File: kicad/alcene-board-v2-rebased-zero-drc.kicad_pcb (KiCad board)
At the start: 2 copper layers, 123 x 90 mm, 16 parts, among them J1 ESP32-S3-DevKitC-1_J1, J2 USB-C Input, J3 ESP32-S3-DevKitC-1_J3, J4 ILI9341_TFT_14pin, J5 Male Pin Header 1x18 - J1 Sig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, J6 Male Pin Header 1x18 - J3 Sig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, J7 Male Pin Header 2x4 - GND, J8 Male Pin Header 2x4 - 3V3, J9 Male Pin Header 2x4 - VIN 5V, SW1 ESP32-S3 Reset (NO momentary)

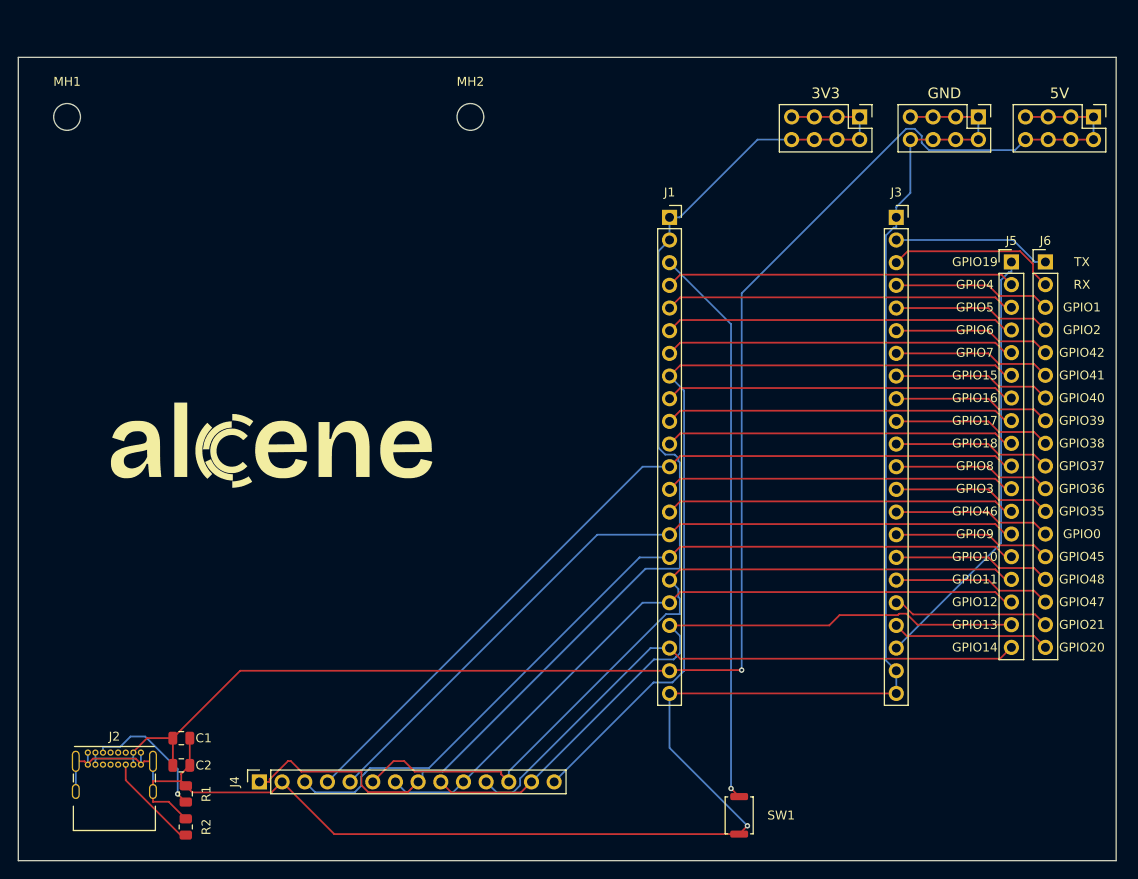
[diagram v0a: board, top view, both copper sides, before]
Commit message: feat: Update component positions and increase fabrication line widths in PCB l
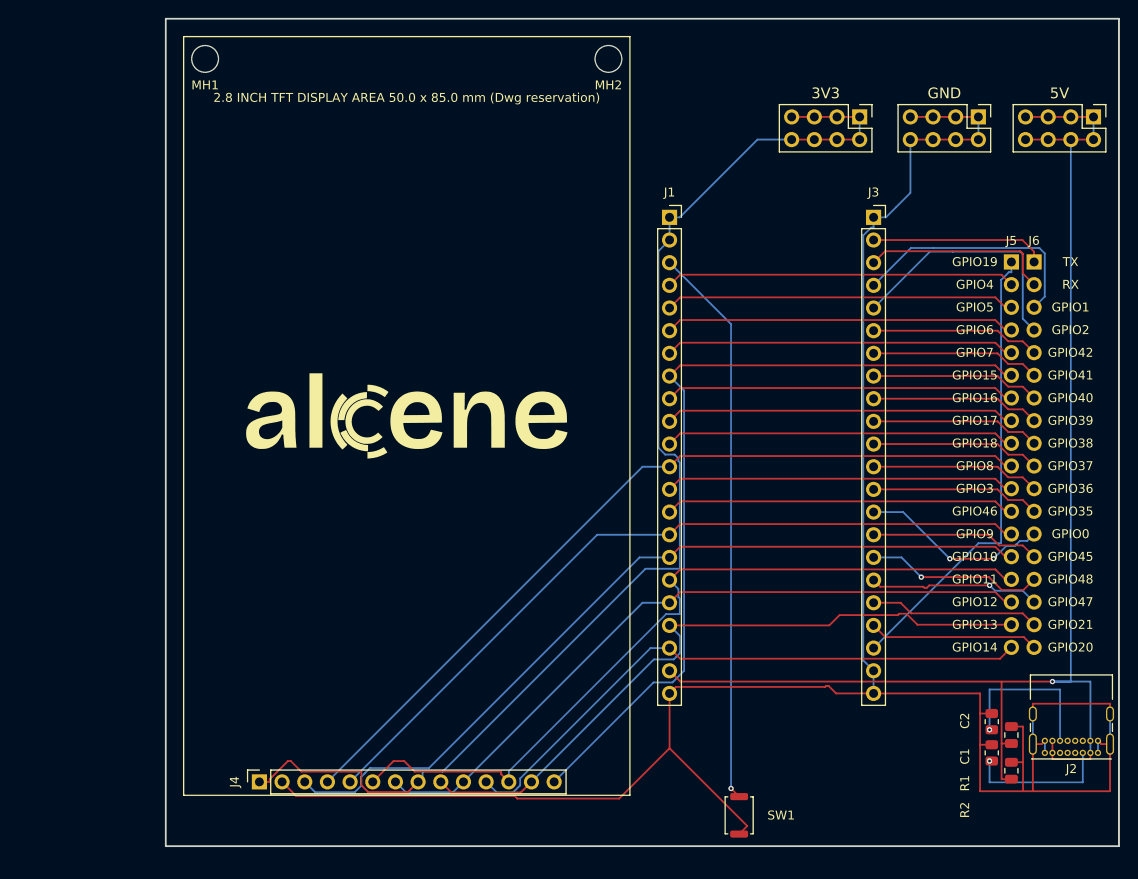
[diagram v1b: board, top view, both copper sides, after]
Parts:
- moved J2 113.2 mm to (154.7, 110.0), turned to 180 degrees
- moved C1 93.1 mm to (145.0, 112.0), turned to 90 degrees
- moved C2 93.1 mm to (145.0, 108.0), turned to 90 degrees
- moved R2 91.1 mm to (142.8, 106.5)
- moved R1 90.4 mm to (142.8, 110.0)
- moved MH2 16.8 mm to (99.9, 32.2)
- moved MH1 16.8 mm to (54.7, 32.2)
- moved J3 2.54 mm to (129.6, 50.0)
- moved J6 1.27 mm to (147.5, 55.0)
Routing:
- net GND: track 226.9 -> 257.2 mm, vias 1 -> 0
- net VIN: track 183.4 -> 156.3 mm
- net GPIO2: track 17.7 -> 28.5 mm
- net GPIO1: track 17.7 -> 27.7 mm
- net Net-(J2-PadB5): track 11.0 -> 18.2 mm, vias 0 -> 1
- net GPIO0: track 17.7 -> 21.3 mm, vias 0 -> 2
- net GPIO19: track 48.8 -> 51.3 mm
- net GPIO48: track 17.7 -> 20.0 mm, vias 0 -> 1
- net RX: track 19.3 -> 21.4 mm
- net TX: track 17.7 -> 19.7 mm
- net GPIO47: track 17.7 -> 19.2 mm, vias 0 -> 1
- net GPIO21: track 17.7 -> 19.0 mm
- net GPIO45: track 17.7 -> 19.0 mm
- net GPIO38: track 17.7 -> 19.0 mm
- net GPIO36: track 17.7 -> 19.0 mm
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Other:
- board size 123 x 90 mm -> 106.8 x 92.7 mm
- board text added: "2.8 INCH TFT DISPLAY AREA 50.0 x 85.0 mm (Dwg reservation)"
- board text removed: "2.8 INCH TFT DISPLAY AREA 49.8 x 78.5 mm (Dwg reservation)"

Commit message: feat: Align power breakout headers and update project configuration
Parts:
- moved J8 13.7 mm to (114.3, 38.8)
- moved J7 10.4 mm to (130.9, 38.8)
- moved J9 6.66 mm to (147.5, 38.8)
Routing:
- net 3V3: track 137.9 -> 129.3 mm
- net VIN: track 156.3 -> 160.5 mm
- net GND: track 257.2 -> 260.9 mm
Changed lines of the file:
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@@
 	(footprint "Connector_PinHeader_2.54mm:PinHeader_2x04_P2.54mm_Vertical"
 		(layer "F.Cu")
-		(at 128 38.75 -90)
+		(at 114.32 38.75 -90)
 		(descr "Through hole straight pin header, 2x04, 2.54mm pitch, double rows")
 		(tags "Through hole pin header THT 2x04 2.54mm double row")
@@
 	(footprint "Connector_PinHeader_2.54mm:PinHeader_2x04_P2.54mm_Vertical"
 		(layer "F.Cu")
-		(at 141.3 38.75 -90)
+		(at 130.93 38.75 -90)
 		(descr "Through hole straight pin header, 2x04, 2.54mm pitch, double rows")
 		(tags "Through hole pin header THT 2x04 2.54mm double row")
@@
 	(footprint "Connector_PinHeader_2.54mm:PinHeader_2x04_P2.54mm_Vertical"
 		(layer "F.Cu")
-		(at 154.2 38.75 -90)
+		(at 147.54 38.75 -90)
 		(descr "Through hole straight pin header, 2x04, 2.54mm pitch, double rows")
 		(tags "Through hole pin header THT 2x04 2.54mm double row")
@@
 	)
 	(gr_text "3V3"
-		(at 124.19 36.1 0)
+		(at 110.51 36.1 0)
 		(layer "F.SilkS")
 		(effects
@@
 	)
 	(gr_text "GND"
-		(at 137.49 36.1 0)
+		(at 127.12 36.1 0)
 		(layer "F.SilkS")
 		(effects
@@
 	)
 	(gr_text "5V"
-		(at 150.39 36.1 0)
+		(at 143.73 36.1 0)
 		(layer "F.SilkS")
 		(effects
@@
 	)
 	(segment
-		(start 136.22 41.29)
-		(end 138.76 41.29)
-		(width 0.2)
-		(layer "F.Cu")
-		(net "GND")
-	)
-	(segment
-		(start 138.76 38.75)
-		(end 141.3 38.75)
-		(width 0.2)
-		(layer "F.Cu")
-		(net "GND")
-	)
-	(segment
 		(start 124.237 102.496)
 		(end 124.12 102.613)
@@
 	)
 	(segment
-		(start 138.76 41.29)
-		(end 141.3 41.29)
-		(width 0.2)
-		(layer "F.Cu")
-		(net "GND")
-	)
-	(segment
-		(start 136.22 38.75)
-		(end 138.76 38.75)
-		(width 0.2)
-		(layer "F.Cu")
-		(net "GND")
-	)
-	(segment
 		(start 64.8762 114.836)
 		(end 71.9021 114.836)
@@
 	)
 	(segment
-		(start 133.68 41.29)
-		(end 136.22 41.29)
-		(width 0.2)
-		(layer "F.Cu")
-		(net "GND")
-	)
-	(segment
 		(start 147.4 105.64)
 		(end 147.4 104.488)
@@
 	)
 	(segment
-		(start 133.68 38.75)
-		(end 136.22 38.75)
-		(width 0.2)
-		(layer "F.Cu")
-		(net "GND")
-	)
-	(segment
 		(start 89.3636 114.836)
 		(end 89.6451 115.118)
@@
 	)
 	(segment
-		(start 129.56 50)
-		(end 130.948 50)
-		(width 0.2)
-		(layer "B.Cu")
-		(net "GND")
-	)
-	(segment
-		(start 130.948 50)
-		(end 132.1 48.8483)
-		(width 0.2)
-		(layer "B.Cu")
-		(net "GND")
-	)
-	(segment
 		(start 148.75 108.65)
 		(end 148.75 110)
@@
 	)
 	(segment
-		(start 141.3 41.29)
-		(end 141.3 38.75)
-		(width 0.2)
-		(layer "B.Cu")
-		(net "GND")
-	)
-	(segment
 		(start 128.402 99.6419)
 		(end 129.56 100.8)
@@
 	)
 	(segment
-		(start 133.68 47.2683)
-		(end 132.1 48.8483)
-		(width 0.2)
-		(layer "B.Cu")
-		(net "GND")
-	)
-	(segment
 		(start 129.56 103.34)
 		(end 129.56 100.8)
@@
 	)
 	(segment
-		(start 133.68 41.29)
-		(end 133.68 47.2683)
-		(width 0.2)
-		(layer "B.Cu")
-		(net "GND")
-	)
-	(segment
 		(start 129.272 51.1517)
 		(end 128.402 52.0219)
@@
 	)
 	(segment
-		(start 146.58 41.29)
-		(end 149.12 41.29)
-		(width 0.2)
-		(layer "F.Cu")
-		(net "VIN")
-	)
-	(segment
-		(start 151.66 38.75)
-		(end 154.2 38.75)
-		(width 0.2)
-		(layer "F.Cu")
-		(net "VIN")
-	)
-	(segment
-		(start 149.12 41.29)
-		(end 151.66 41.29)
-		(width 0.2)
-		(layer "F.Cu")
-		(net "VIN")
-	)
-	(segment
-		(start 146.58 38.75)
-		(end 149.12 38.75)
-		(width 0.2)
-		(layer "F.Cu")
-		(net "VIN")
-	)
-	(segment
-		(start 151.66 41.29)
-		(end 154.2 41.29)
-		(width 0.2)
-		(layer "F.Cu")
-		(net "VIN")
-	)
-	(segment
-		(start 149.12 38.75)
-		(end 151.66 38.75)
-		(width 0.2)
-		(layer "F.Cu")
-		(net "VIN")
-	)
-	(segment
 		(start 106.7 100.8)
 		(end 107.913 102.013)
@@
 	)
 	(segment
-		(start 154.2 41.29)
-		(end 154.2 38.75)
-		(width 0.2)
-		(layer "B.Cu")
-		(net "VIN")
-	)
-	(segment
 		(start 151.66 41.29)
 		(end 151.66 102.013)
@@
 	)
 	(segment
-		(start 125.46 38.75)
-		(end 128 38.75)
-		(width 0.2)
-		(layer "F.Cu")
-		(net "3V3")
-	)
-	(segment
 		(start 64.2737 110.923)
 		(end 63.9409 110.923)
@@
 	)
 	(segment
-		(start 122.92 41.29)
-		(end 125.46 41.29)
-		(width 0.2)
-		(layer "F.Cu")
-		(net "3V3")
-	)
-	(segment
 		(start 72.18 113.634)
 		(end 72.18 112.1)
@@
 	)
 	(segment
-		(start 125.46 41.29)
-		(end 128 41.29)
-		(width 0.2)
-		(layer "F.Cu")
-		(net "3V3")
-	)
-	(segment
 		(start 60.75 113.25)
 		(end 61.9017 113.25)
@@
 	)
 	(segment
-		(start 122.92 38.75)
-		(end 125.46 38.75)
-		(width 0.2)
-		(layer "F.Cu")
-		(net "3V3")
-	)
-	(segment
-		(start 120.38 41.29)
-		(end 122.92 41.29)
-		(width 0.2)
-		(layer "F.Cu")
-		(net "3V3")
-	)
-	(segment
 		(start 72.9474 114.402)
 		(end 72.18 113.634)
@@
 	)
 	(segment
-		(start 120.38 38.75)
-		(end 122.92 38.75)
-		(width 0.2)
-		(layer "F.Cu")
-		(net "3V3")
-	)
-	(segment
 		(start 79.0271 112.1)
 		(end 81.2742 112.1)
@@
 	)
 	(segment
-		(start 106.7 50)
-		(end 107.852 50)
-		(width 0.2)
-		(layer "B.Cu")
-		(net "3V3")
-	)
-	(segment
 		(start 105.46 53.7799)
 		(end 106.7 52.54)
@@
 	)
 	(segment
-		(start 128 41.29)
-		(end 128 38.75)
-		(width 0.2)
-		(layer "B.Cu")
-		(net "3V3")
-	)
-	(segment
 		(start 106.214 76.5803)
 		(end 105.46 75.8263)
@@
 	)
 	(segment
-		(start 120.38 41.29)
-		(end 116.562 41.29)
-		(width 0.2)
-		(layer "B.Cu")
-		(net "3V3")
-	)
-	(segment
 		(start 106.7 52.54)
 		(end 106.7 50)
@@
 	)
 	(segment
-		(start 116.562 41.29)
-		(end 107.852 50)
-		(width 0.2)
-		(layer "B.Cu")
-		(net "3V3")
-	)
-	(segment
 		(start 79.0271 112.753)
 		(end 79.0271 112.1)
@@
 		(net "VIN")
 	)
+(segment
+		(start 106.7 38.75)
+		(end 114.32 38.75)
+		(width 0.2)
+		(layer "F.Cu")
+		(net "3V3")
+	)
+(segment
+		(start 106.7 41.29)
+		(end 114.32 41.29)
+		(width 0.2)
+		(layer "F.Cu")
+		(net "3V3")
+	)
+(segment
+		(start 114.32 41.29)
+		(end 114.32 38.75)
+		(width 0.2)
+		(layer "B.Cu")
+		(net "3V3")
+	)
+(segment
+		(start 106.7 50)
+		(end 106.7 41.29)
+		(width 0.2)
+		(layer "B.Cu")
+		(net "3V3")
+	)
+(segment
+		(start 139.92 38.75)
+		(end 147.54 38.75)
+		(width 0.2)
+		(layer "F.Cu")
+		(net "VIN")
+	)
+(segment
+		(start 139.92 41.29)
+		(end 147.54 41.29)
+		(width 0.2)
+		(layer "F.Cu")
+		(net "VIN")
+	)
+(segment
+		(start 147.54 41.29)
+		(end 147.54 38.75)
+		(width 0.2)
+		(layer "B.Cu")
+		(net "VIN")
+	)
+(segment
+		(start 147.54 41.29)
+		(end 151.66 41.29)
+		(width 0.2)
+		(layer "B.Cu")
+		(net "VIN")
+	)
+(segment
+		(start 123.31 38.75)
+		(end 130.93 38.75)
+		(width 0.2)
+		(layer "F.Cu")
+		(net "GND")
+	)
+(segment
+		(start 123.31 41.29)
+		(end 130.93 41.29)
+		(width 0.2)
+		(layer "F.Cu")
+		(net "GND")
+	)
+(segment
+		(start 130.93 41.29)
+		(end 130.93 38.75)
+		(width 0.2)
+		(layer "B.Cu")
+		(net "GND")
+	)
+(segment
+		(start 129.56 50)
+		(end 129.56 44.31)
+		(width 0.2)
+		(layer "B.Cu")
+		(net "GND")
+	)
+(segment
+		(start 123.31 44.31)
+		(end 129.56 44.31)
+		(width 0.2)
+		(layer "B.Cu")
+		(net "GND")
+	)
+(segment
+		(start 123.31 41.29)
+		(end 123.31 44.31)
+		(width 0.2)
+		(layer "B.Cu")
+		(net "GND")
+	)
 	(embedded_fonts no)

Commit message: feat: reorrient USB C
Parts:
- moved J2 11.6 mm to (143.3, 111.8), turned to 0 degrees
- moved R2 7.40 mm to (149.9, 108.6)
- moved C2 6.93 mm to (151.9, 108.6)
- moved C1 4.40 mm to (147.8, 108.6)
- moved R1 2.60 mm to (145.0, 108.6)
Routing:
- net GND: track 260.9 -> 239.8 mm, vias 0 -> 1
- net Net-(J2-PadA5): track 16.1 -> 2.33 mm, vias 1 -> 0
- net Net-(J2-PadB5): track 18.2 -> 10.9 mm, vias 1 -> 0
- net VIN: track 160.5 -> 167.7 mm

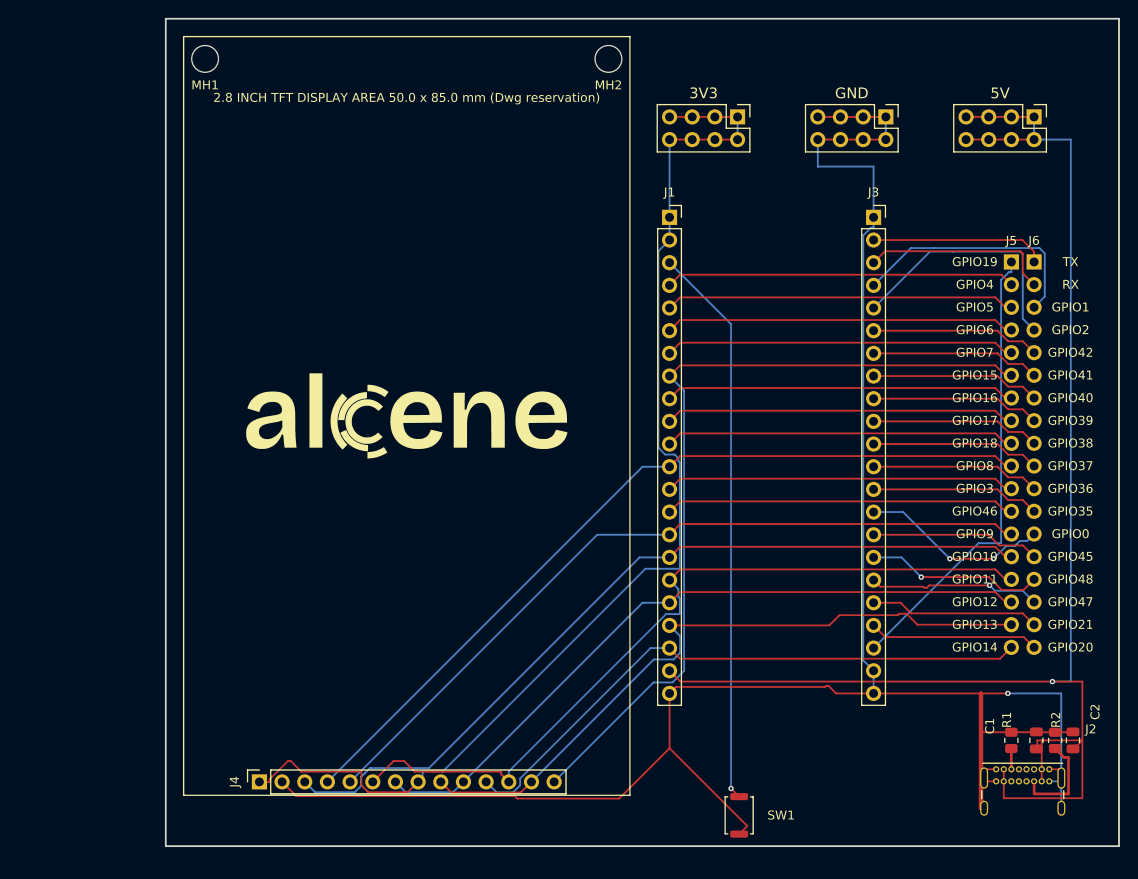
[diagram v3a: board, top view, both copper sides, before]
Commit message: feat: Shift PCB components and traces by 2.54mm to the left
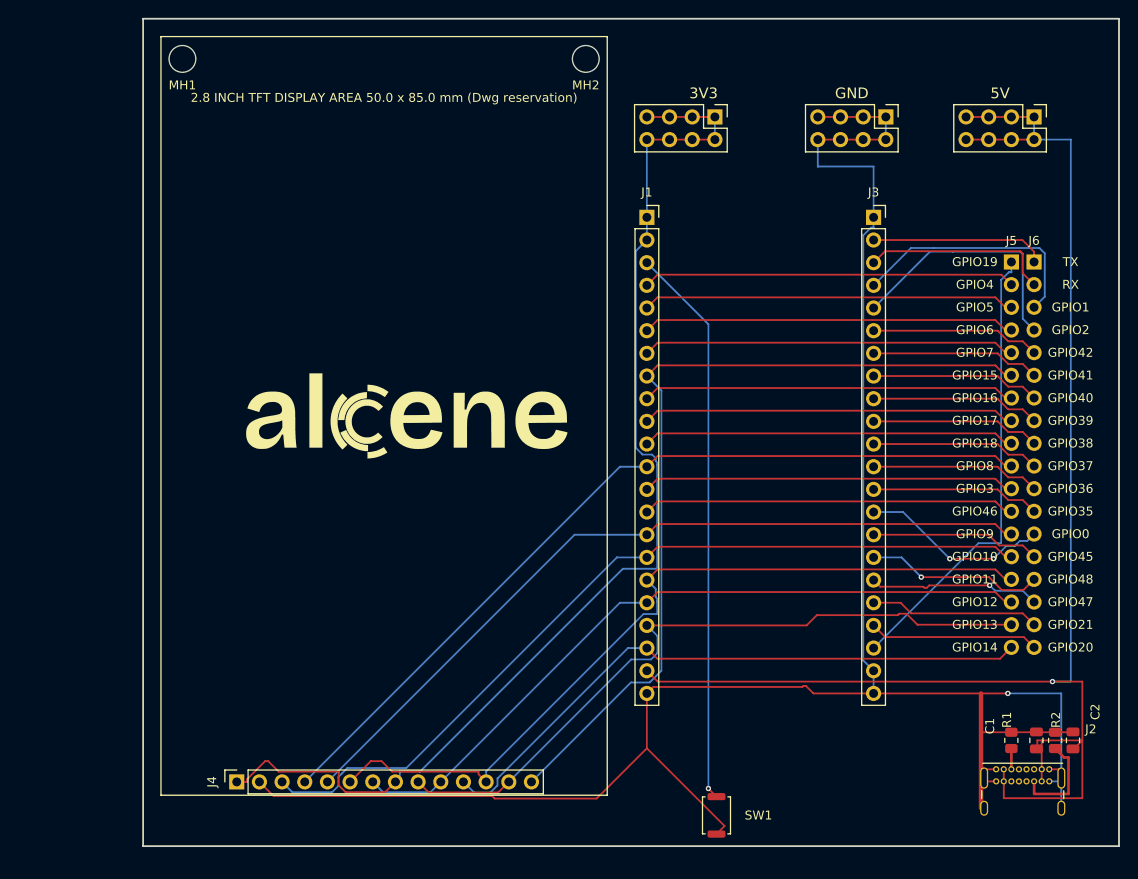
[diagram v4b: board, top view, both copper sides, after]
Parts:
- moved J1 2.54 mm to (104.2, 50.0)
- moved MH2 2.54 mm to (97.3, 32.2)
- moved SW1 2.54 mm to (112.0, 117.0)
- moved J4 2.54 mm to (58.2, 113.2)
- moved MH1 2.54 mm to (52.1, 32.2)
- moved J8 2.54 mm to (111.8, 38.8)
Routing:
- net GPIO15: track 92.7 -> 95.2 mm
- net GPIO14: track 67.5 -> 70.1 mm
- net GPIO11: track 88.6 -> 91.1 mm
- net GPIO7: track 39.3 -> 41.8 mm
- net GPIO6: track 39.3 -> 41.8 mm
- net GPIO5: track 39.3 -> 41.8 mm
- net GPIO46: track 39.3 -> 41.8 mm
- net GPIO4: track 39.3 -> 41.8 mm
- net GPIO3: track 39.3 -> 41.8 mm
- net GPIO18: track 39.3 -> 41.8 mm
- net GPIO17: track 39.3 -> 41.8 mm
- net GPIO16: track 39.3 -> 41.8 mm
- net VIN: track 167.7 -> 170.2 mm
- net GPIO9: track 86.5 -> 89.1 mm
- net GPIO8: track 92.2 -> 94.8 mm
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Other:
- board size 106.8 x 92.7 mm -> 109.3 x 92.7 mm

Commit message: feat: Update mounting hole positions and adjust component footprints
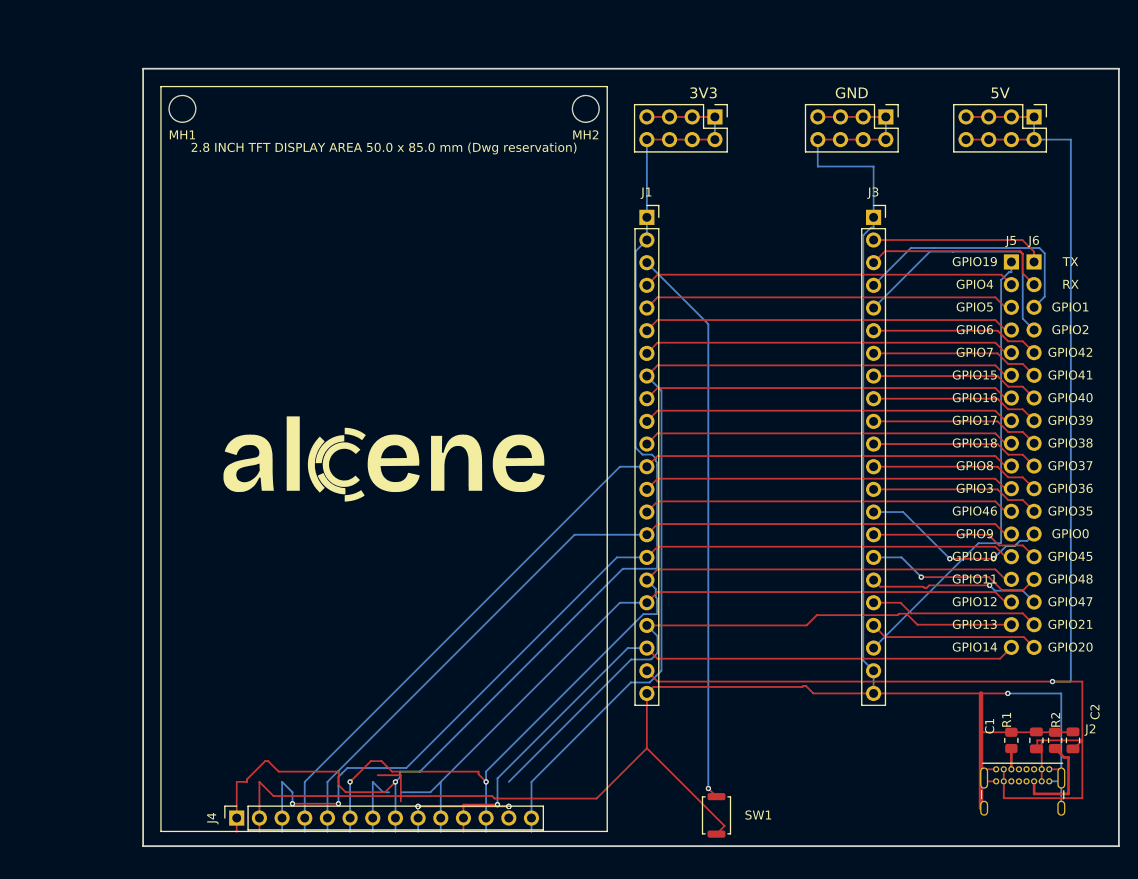
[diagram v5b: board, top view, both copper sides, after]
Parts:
- moved MH1 5.60 mm to (52.1, 37.9)
- moved MH2 5.60 mm to (97.3, 37.9)
- moved J4 4.05 mm to (58.2, 117.3)
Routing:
- net GPIO11: track 91.1 -> 102.3 mm, vias 0 -> 2
- net 3V3: track 129.3 -> 140.5 mm, vias 0 -> 1
- net GND: track 242.4 -> 253.5 mm
- net GPIO12: track 81.8 -> 91.6 mm
- net GPIO10: track 94.6 -> 103.2 mm, vias 0 -> 2
- net GPIO9: track 89.1 -> 94.7 mm
- net GPIO8: track 94.8 -> 100.4 mm
- net GPIO15: track 95.2 -> 100.8 mm
- net GPIO14: track 70.1 -> 74.4 mm, vias 0 -> 1
- net GPIO13: track 79.3 -> 81.1 mm, vias 0 -> 4
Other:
- board size 109.3 x 92.7 mm -> 109.3 x 87.1 mm
